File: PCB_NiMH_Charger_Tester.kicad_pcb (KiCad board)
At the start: 2 copper layers, 94.9 x 77.5 mm, 63 parts, among them J1 USB_C_Receptacle_PowerOnly_6P, J2 USB_C_Receptacle_USB2.0_16P, J3 UPDI v2 header, J4 SSD1306, J5 Serial Header, Q1 DTC114EL, Q2 DTA114EL, Q3 MTB060P06I3, Q4 MTA100N10KRI3, SW1 SW_Push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

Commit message: Update silk
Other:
- board text added: "Chg/↑"
- board text added: "Dis/↓"
- board text added: "Menu/OK"
- board text added: "https://github.com/k-takata/PCB_NiMH_Charger_Tester"
- board text removed: "WayWayWay"
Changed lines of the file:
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@@
+		)
+	)
+	(gr_text "Chg/↑"
+		(at 61.595 100.33 0)
+		(layer "F.SilkS")
+		(effects
+			(font
+				(size 1 1)
+				(thickness 0.15)
+			)
+			(justify left bottom)
+		)
+	)
+	(gr_text "Dis/↓"
+		(at 72.136 100.33 0)
+		(layer "F.SilkS")
+		(effects
+			(font
+				(size 1 1)
+				(thickness 0.15)
+			)
+			(justify left bottom)
 		)
 	)
@@
 		)
 	)
+	(gr_text "Menu/OK"
+		(at 80.772 100.33 0)
+		(layer "F.SilkS")
+		(effects
+			(font
+				(size 1 1)
+				(thickness 0.15)
+			)
+			(justify left bottom)
+		)
+	)
 	(gr_text "+"
 		(at 50.165 49.53 270)
@@
 		)
 	)
-	(gr_text "WayWayWay"
-		(at 131.445 99.06 0)
+	(gr_text "https://github.com/k-takata/PCB_NiMH_Charger_Tester"
+		(at 141.224 78.994 0)
 		(layer "B.SilkS")
 		(effects
 			(font
-				(size 1 1)
+				(size 1 0.8)
 				(thickness 0.1)
 			)

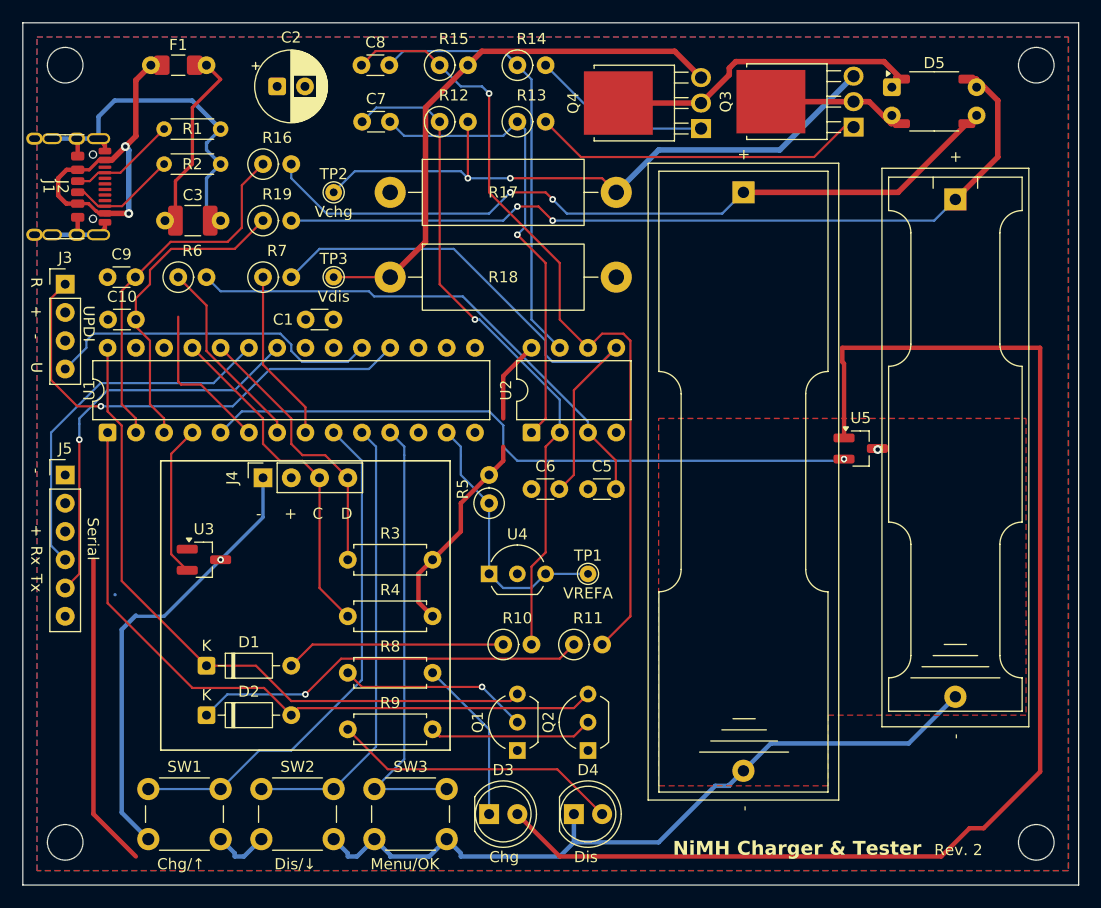
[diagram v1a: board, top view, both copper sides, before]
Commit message: Connect Vchg/Vdis to AVR
Also, change J3/J5 direction.
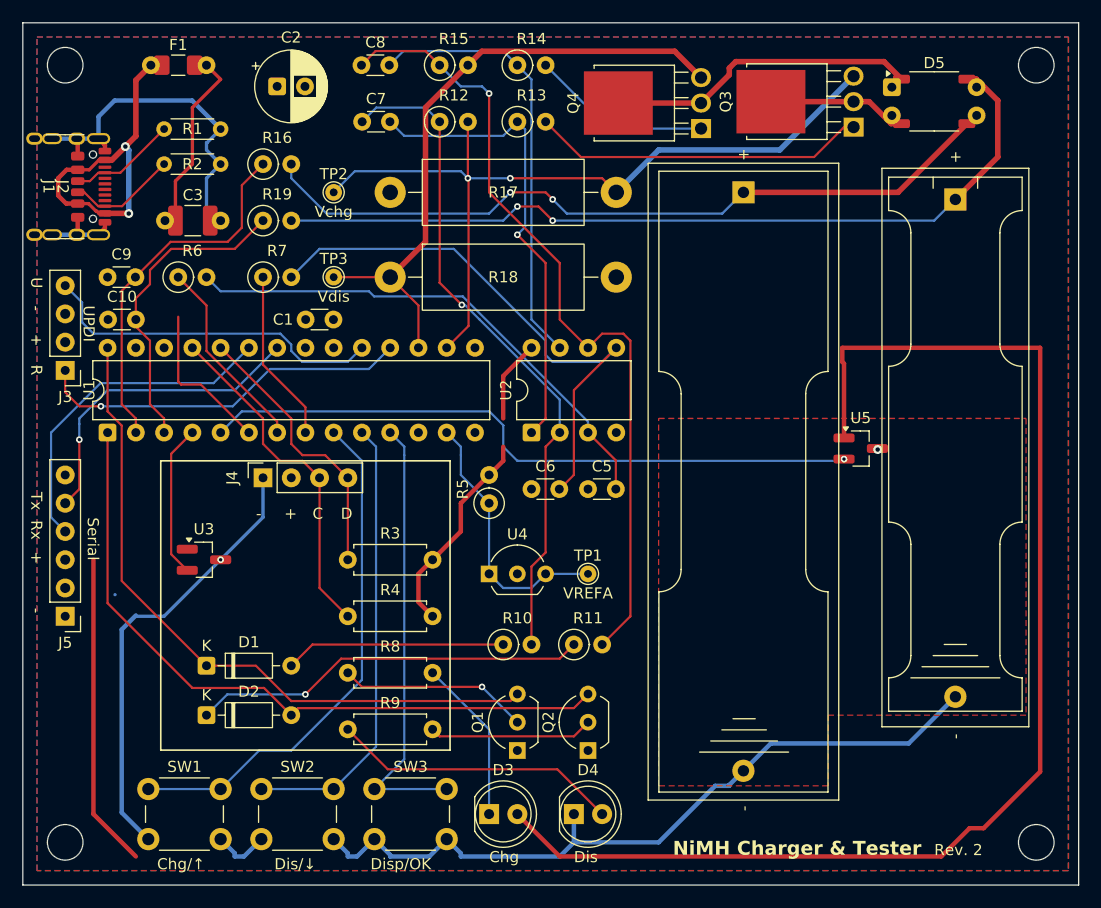
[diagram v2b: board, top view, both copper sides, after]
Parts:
- moved J5 12.7 mm to (53.3, 77.5), turned to 180 degrees
- moved J3 7.75 mm to (53.3, 55.4), turned to 180 degrees
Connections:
- Q3 pad 3: Net-(Q3-S) -> Vchg
- Q4 pad 3: Net-(Q4-S) -> Vdis
- R12 pad 2: Net-(Q3-S) -> Vchg
- R15 pad 2: Net-(Q4-S) -> Vdis
- R17 pad 2: Net-(Q3-S) -> Vchg
- R18 pad 1: Net-(Q4-S) -> Vdis
- TP2 pad 1: Net-(Q3-S) -> Vchg
- TP3 pad 1: Net-(Q4-S) -> Vdis
- U1 pad 16: unconnected-(U1-XTAL32K1/PF0-Pad16) -> Vchg
- U1 pad 17: unconnected-(U1-XTAL32K2/PF1-Pad17) -> Vdis
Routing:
- net Vchg: track 0.00 -> 73.8 mm, vias 0 -> 2
- net Net-(Q3-S): track 57.7 -> 0.00 mm, vias 2 -> 0
- net Vdis: track 0.00 -> 56.9 mm
- net Net-(Q4-S): track 49.5 -> 0.00 mm
- net RESET: track 42.8 -> 33.9 mm
- net TX: track 36.2 -> 28.6 mm
- net RX: track 32.9 -> 30.4 mm
- net UPDI: track 30.3 -> 31.4 mm
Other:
- board text added: "Disp/OK"
- board text removed: "Menu/OK"

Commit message: Update button name
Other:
- board text added: "Mode/OK"
- board text removed: "Disp/OK"
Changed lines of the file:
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@@
 		)
 	)
-	(gr_text "Disp/OK"
+	(gr_text "Mode/OK"
 		(at 80.772 100.33 0)
 		(layer "F.SilkS")
